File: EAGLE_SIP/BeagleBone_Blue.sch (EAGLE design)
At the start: 266 parts, among them M1 JST_ZH_2, M2 JST_ZH_2, M3 JST_ZH_2, M4 JST_ZH_2, P10 SCHA5B0200, Q3 MOSFET-N, U1 TPD4S012_DRY_6, U4 TPD4S012_DRY_6, U5 24LC_32AT-I/OT, U6 SN74LVC1G07_DCK_5, U7 TPS2051B_D_8, U8 MTFC4GLDEA, Y1 CM200C-32.768KAZF-UT, Y2 445C33D24M00000

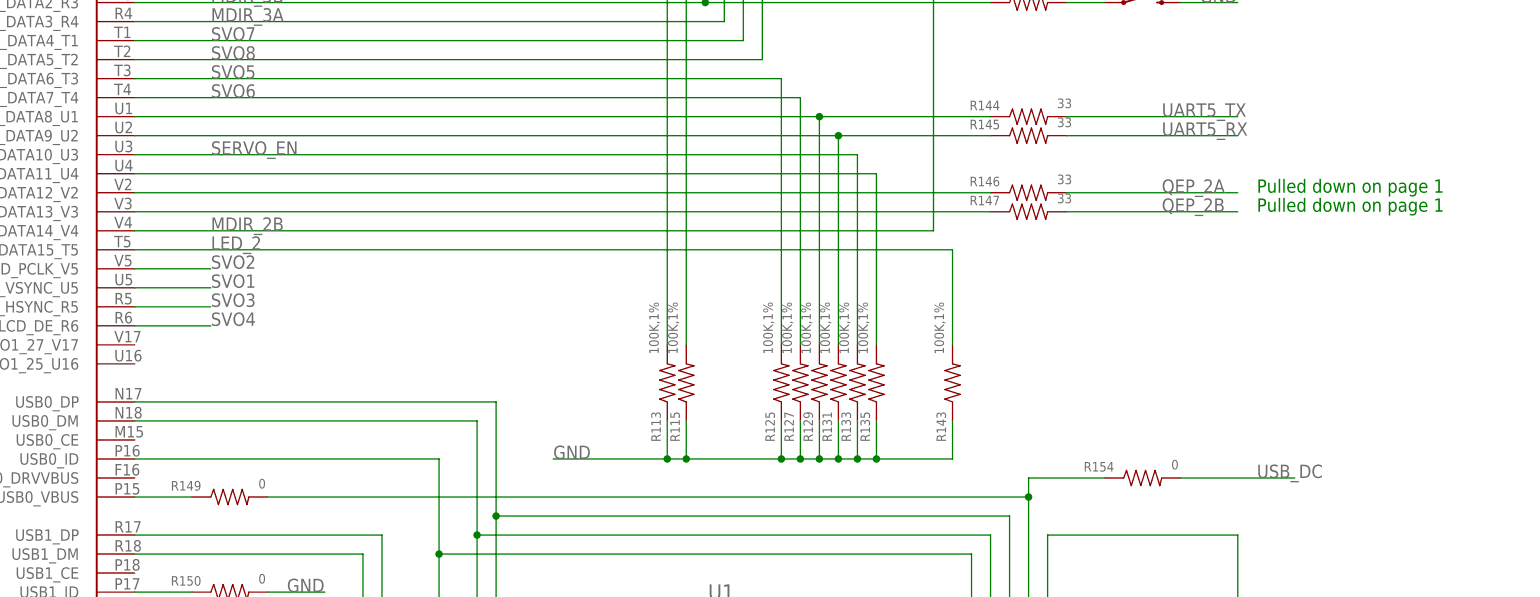
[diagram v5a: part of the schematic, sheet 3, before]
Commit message: Remove redundant pull-down resistor R133
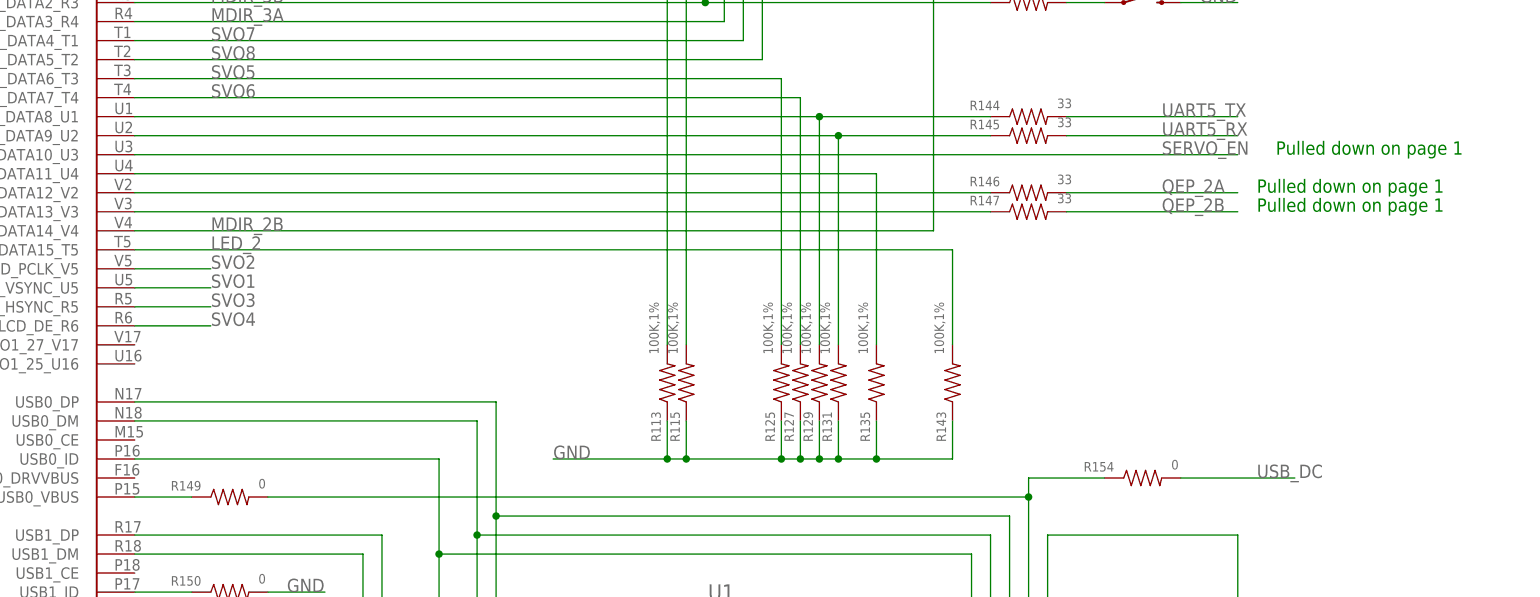
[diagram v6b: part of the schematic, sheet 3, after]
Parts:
- removed R133: 100K,1%, Strawson_Eagle_Lib:RESISTOR0402-RES
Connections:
- net GND: no longer R133.1
- net SERVO_EN: no longer R133.2
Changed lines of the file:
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@@
 <part name="R129" library="Strawson_Eagle_Lib" deviceset="RESISTOR" device="0402-RES" value="100K,1%"/>
 <part name="R131" library="Strawson_Eagle_Lib" deviceset="RESISTOR" device="0402-RES" value="100K,1%"/>
-<part name="R133" library="Strawson_Eagle_Lib" deviceset="RESISTOR" device="0402-RES" value="100K,1%"/>
 <part name="R135" library="Strawson_Eagle_Lib" deviceset="RESISTOR" device="0402-RES" value="100K,1%"/>
 <part name="R140" library="Strawson_Eagle_Lib" deviceset="RESISTOR" device="0402-RES" value="100K,1%"/>
@@
 <text x="340.36" y="167.64" size="1.778" layer="91">Pulled down on page 1</text>
 <text x="340.36" y="165.1" size="1.778" layer="91">Pulled down on page 1</text>
+<text x="342.9" y="172.72" size="1.778" layer="91">Pulled down on page 1</text>
 </plain>
 <instances>
@@
 <attribute name="VALUE" x="282.702" y="146.05" size="1.27" layer="96" rot="R90" align="center-left"/>
 </instance>
-<instance part="R133" gate="G$1" x="287.02" y="142.24" smashed="yes" rot="R90">
-<attribute name="NAME" x="285.5214" y="138.43" size="1.27" layer="95" rot="R90" align="center-right"/>
-<attribute name="VALUE" x="285.242" y="146.05" size="1.27" layer="96" rot="R90" align="center-left"/>
-</instance>
 <instance part="R135" gate="G$1" x="289.56" y="142.24" smashed="yes" rot="R90">
 <attribute name="NAME" x="288.0614" y="138.43" size="1.27" layer="95" rot="R90" align="center-right"/>
@@
 <wire x1="284.48" y1="132.08" x2="284.48" y2="137.16" width="0.1524" layer="91"/>
 <junction x="281.94" y="132.08"/>
-<pinref part="R133" gate="G$1" pin="1"/>
-<wire x1="284.48" y1="132.08" x2="287.02" y2="132.08" width="0.1524" layer="91"/>
-<wire x1="287.02" y1="132.08" x2="287.02" y2="137.16" width="0.1524" layer="91"/>
 <junction x="284.48" y="132.08"/>
 <pinref part="R135" gate="G$1" pin="1"/>
-<wire x1="287.02" y1="132.08" x2="289.56" y2="132.08" width="0.1524" layer="91"/>
+<wire x1="284.48" y1="132.08" x2="289.56" y2="132.08" width="0.1524" layer="91"/>
 <wire x1="289.56" y1="132.08" x2="289.56" y2="137.16" width="0.1524" layer="91"/>
-<junction x="287.02" y="132.08"/>
 <junction x="289.56" y="132.08"/>
 <pinref part="R143" gate="G$1" pin="1"/>
@@
 <net name="SERVO_EN" class="0">
 <segment>
-<pinref part="R133" gate="G$1" pin="2"/>
 <pinref part="SIP" gate="C" pin="LCD_DATA10_U3"/>
-<wire x1="287.02" y1="172.72" x2="287.02" y2="147.32" width="0.1524" layer="91"/>
-<wire x1="190.5" y1="172.72" x2="287.02" y2="172.72" width="0.1524" layer="91"/>
-<label x="200.66" y="172.72" size="1.778" layer="95"/>
+<wire x1="190.5" y1="172.72" x2="337.82" y2="172.72" width="0.1524" layer="91"/>
+<label x="327.66" y="172.72" size="1.778" layer="95"/>
 </segment>
 </net>

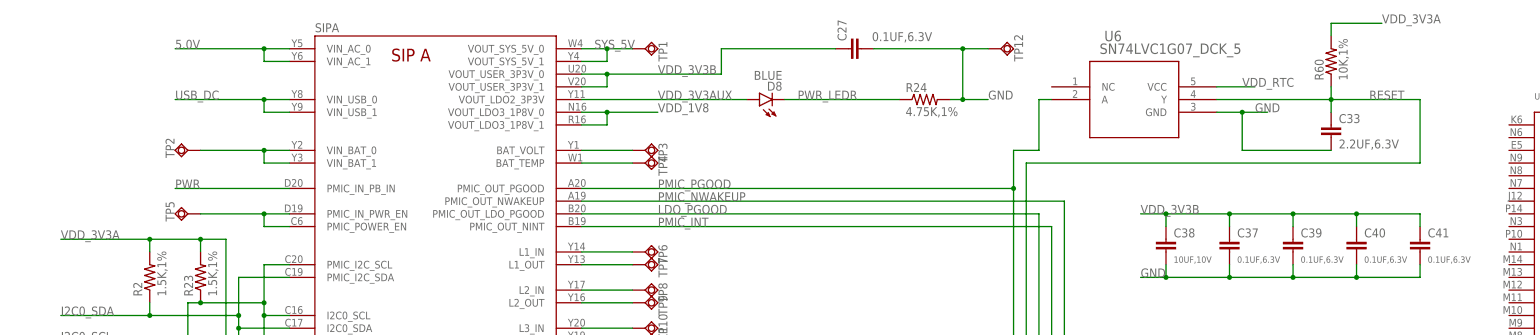
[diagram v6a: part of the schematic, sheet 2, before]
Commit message: Connect VDD_3V3B to 3.3V
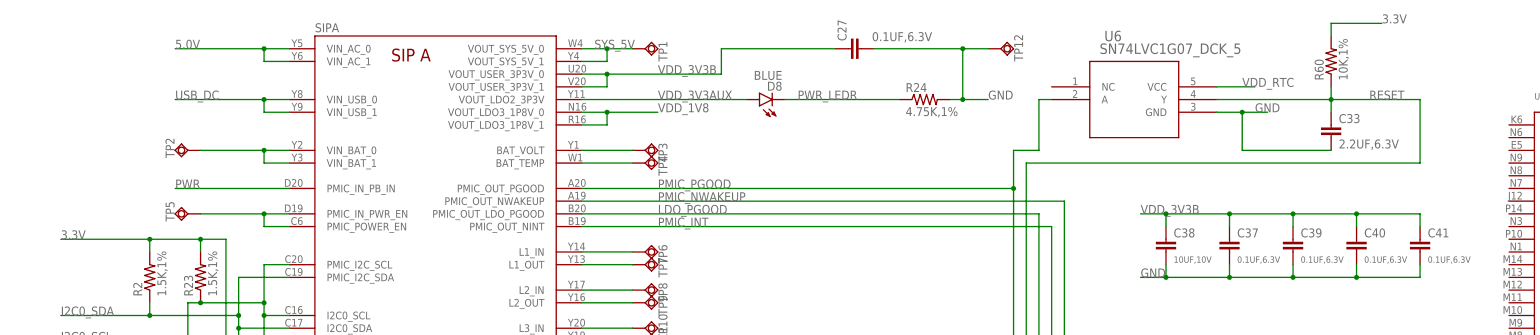
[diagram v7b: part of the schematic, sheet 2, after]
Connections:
- removed net VDD_3V3A: C28.1, R116.2, R118.2, R120.2, R122.2, R140.2, R157.1, R2.2, R23.2, R58.2, R60.2, SIPE.VDD_3V3A1, SIPE.VDD_3V3A10, SIPE.VDD_3V3A11, SIPE.VDD_3V3A12, SIPE.VDD_3V3A13, SIPE.VDD_3V3A14, SIPE.VDD_3V3A15, SIPE.VDD_3V3A16, SIPE.VDD_3V3A17, SIPE.VDD_3V3A18, SIPE.VDD_3V3A19, SIPE.VDD_3V3A2, SIPE.VDD_3V3A20, SIPE.VDD_3V3A21, SIPE.VDD_3V3A3, SIPE.VDD_3V3A4, SIPE.VDD_3V3A5, SIPE.VDD_3V3A6, SIPE.VDD_3V3A7, SIPE.VDD_3V3A8, SIPE.VDD_3V3A9, U5.VCC
- net 3.3V: now also C28.1, R116.2, R118.2, R120.2, R122.2, R140.2, R157.1, R2.2, R23.2, R58.2, R60.2, SIPE.VDD_3V3A1, SIPE.VDD_3V3A10, SIPE.VDD_3V3A11, SIPE.VDD_3V3A12, SIPE.VDD_3V3A13, SIPE.VDD_3V3A14, SIPE.VDD_3V3A15, SIPE.VDD_3V3A16, SIPE.VDD_3V3A17, SIPE.VDD_3V3A18, SIPE.VDD_3V3A19, SIPE.VDD_3V3A2, SIPE.VDD_3V3A20, SIPE.VDD_3V3A21, SIPE.VDD_3V3A3, SIPE.VDD_3V3A4, SIPE.VDD_3V3A5, SIPE.VDD_3V3A6, SIPE.VDD_3V3A7, SIPE.VDD_3V3A8, SIPE.VDD_3V3A9, U5.VCC
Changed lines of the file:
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@@
 </segment>
 </net>
-<net name="VDD_3V3A" class="0">
+<net name="3.3V" class="0">
 <segment>
 <pinref part="R2" gate="G$1" pin="2"/>
@@
 </segment>
 </net>
-<net name="VDD_3V3A" class="0">
+<net name="3.3V" class="0">
 <segment>
 <wire x1="233.68" y1="226.06" x2="266.7" y2="226.06" width="0.1524" layer="91"/>
@@
 </segment>
 </net>
-<net name="VDD_3V3A" class="0">
+<net name="3.3V" class="0">
 <segment>
 <pinref part="SIP" gate="E" pin="VDD_3V3A1"/>

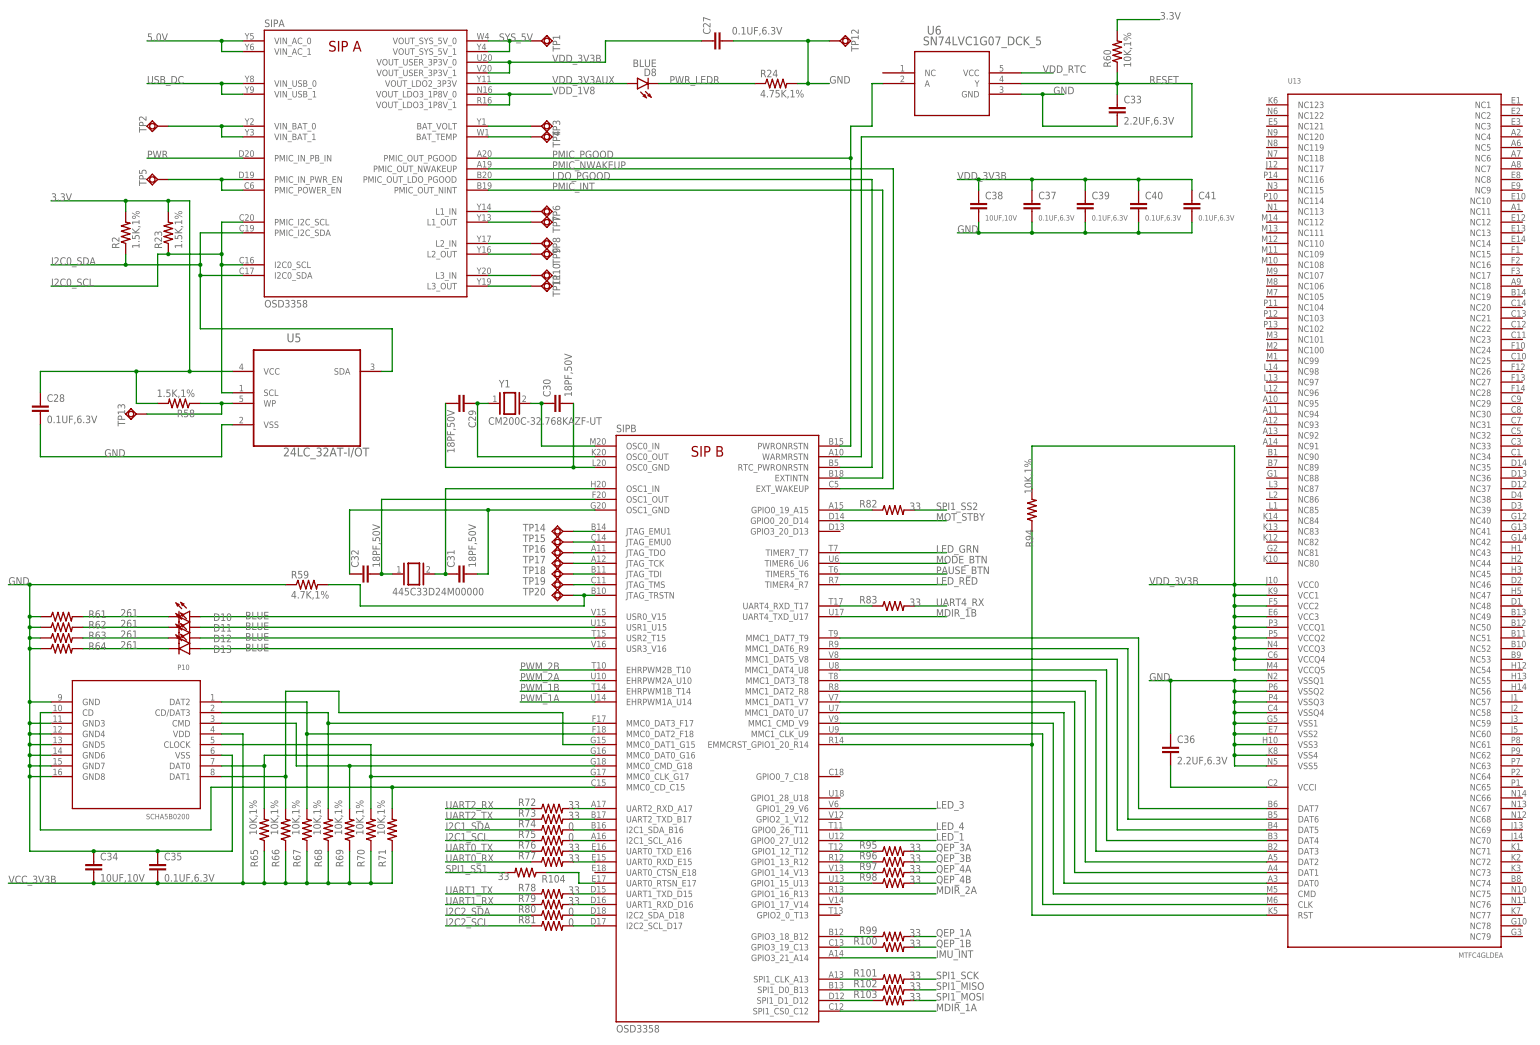
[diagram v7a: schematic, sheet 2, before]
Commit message: Correctly connect VDD_3V3B to 3.3V
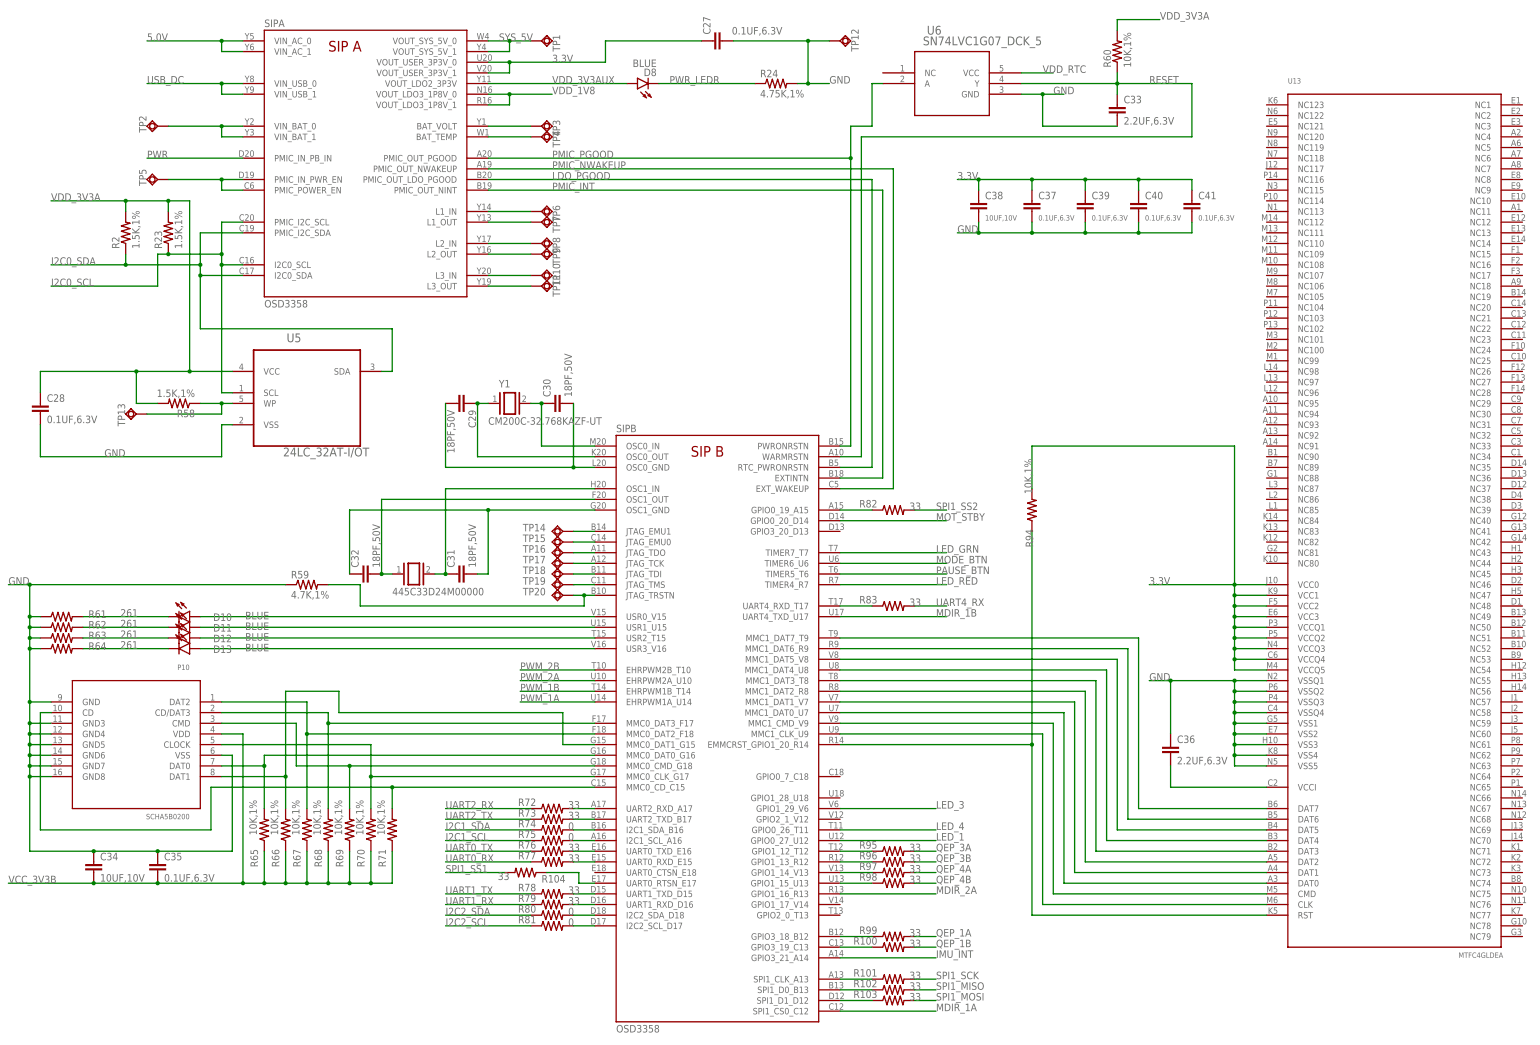
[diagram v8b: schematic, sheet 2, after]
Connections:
- removed net VDD_3V3B: C27.1, C37.1, C38.1, C39.1, C40.1, C41.1, R109.1, R94.2, SIPA.VOUT_USER_3P3V_0, SIPA.VOUT_USER_3P3V_1, U8.VCC0, U8.VCC1, U8.VCC2, U8.VCC3, U8.VCCQ1, U8.VCCQ2, U8.VCCQ3, U8.VCCQ4, U8.VCCQ5
- new net VDD_3V3A: C28.1, R116.2, R118.2, R120.2, R122.2, R140.2, R157.1, R2.2, R23.2, R58.2, R60.2, SIPE.VDD_3V3A1, SIPE.VDD_3V3A10, SIPE.VDD_3V3A11, SIPE.VDD_3V3A12, SIPE.VDD_3V3A13, SIPE.VDD_3V3A14, SIPE.VDD_3V3A15, SIPE.VDD_3V3A16, SIPE.VDD_3V3A17, SIPE.VDD_3V3A18, SIPE.VDD_3V3A19, SIPE.VDD_3V3A2, SIPE.VDD_3V3A20, SIPE.VDD_3V3A21, SIPE.VDD_3V3A3, SIPE.VDD_3V3A4, SIPE.VDD_3V3A5, SIPE.VDD_3V3A6, SIPE.VDD_3V3A7, SIPE.VDD_3V3A8, SIPE.VDD_3V3A9, U5.VCC
- net 3.3V: now also C27.1, C37.1, C38.1, C39.1, C40.1, C41.1, R109.1, R94.2, SIPA.VOUT_USER_3P3V_0, SIPA.VOUT_USER_3P3V_1, U8.VCC0, U8.VCC1, U8.VCC2, U8.VCC3, U8.VCCQ1, U8.VCCQ2, U8.VCCQ3, U8.VCCQ4, U8.VCCQ5; no longer C28.1, R116.2, R118.2, R120.2, R122.2, R140.2, R157.1, R2.2, R23.2, R58.2, R60.2, SIPE.VDD_3V3A1, SIPE.VDD_3V3A10, SIPE.VDD_3V3A11, SIPE.VDD_3V3A12, SIPE.VDD_3V3A13, SIPE.VDD_3V3A14, SIPE.VDD_3V3A15, SIPE.VDD_3V3A16, SIPE.VDD_3V3A17, SIPE.VDD_3V3A18, SIPE.VDD_3V3A19, SIPE.VDD_3V3A2, SIPE.VDD_3V3A20, SIPE.VDD_3V3A21, SIPE.VDD_3V3A3, SIPE.VDD_3V3A4, SIPE.VDD_3V3A5, SIPE.VDD_3V3A6, SIPE.VDD_3V3A7, SIPE.VDD_3V3A8, SIPE.VDD_3V3A9, U5.VCC
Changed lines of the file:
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@@
 </segment>
 </net>
-<net name="3.3V" class="0">
+<net name="VDD_3V3A" class="0">
 <segment>
 <pinref part="R2" gate="G$1" pin="2"/>
@@
 </segment>
 </net>
-<net name="VDD_3V3B" class="0">
+<net name="3.3V" class="0">
 <segment>
 <pinref part="SIP" gate="A" pin="VOUT_USER_3P3V_0"/>
@@
 </segment>
 </net>
-<net name="VDD_3V3B" class="0">
+<net name="3.3V" class="0">
 <segment>
 <wire x1="55.88" y1="177.8" x2="68.58" y2="177.8" width="0.1524" layer="91"/>
@@
 </segment>
 </net>
-<net name="3.3V" class="0">
+<net name="VDD_3V3A" class="0">
 <segment>
 <wire x1="233.68" y1="226.06" x2="266.7" y2="226.06" width="0.1524" layer="91"/>
@@
 </segment>
 </net>
-<net name="3.3V" class="0">
+<net name="VDD_3V3A" class="0">
 <segment>
 <pinref part="SIP" gate="E" pin="VDD_3V3A1"/>
